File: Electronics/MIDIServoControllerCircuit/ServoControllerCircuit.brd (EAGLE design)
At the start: 160 x 100 mm, 19 parts, among them IC1 MCP1700INLINE, J1 PJ-063BH, T1 2N3904, X1 SIGNAL-PWR-GND, X2 SIGNAL-PWR-GND

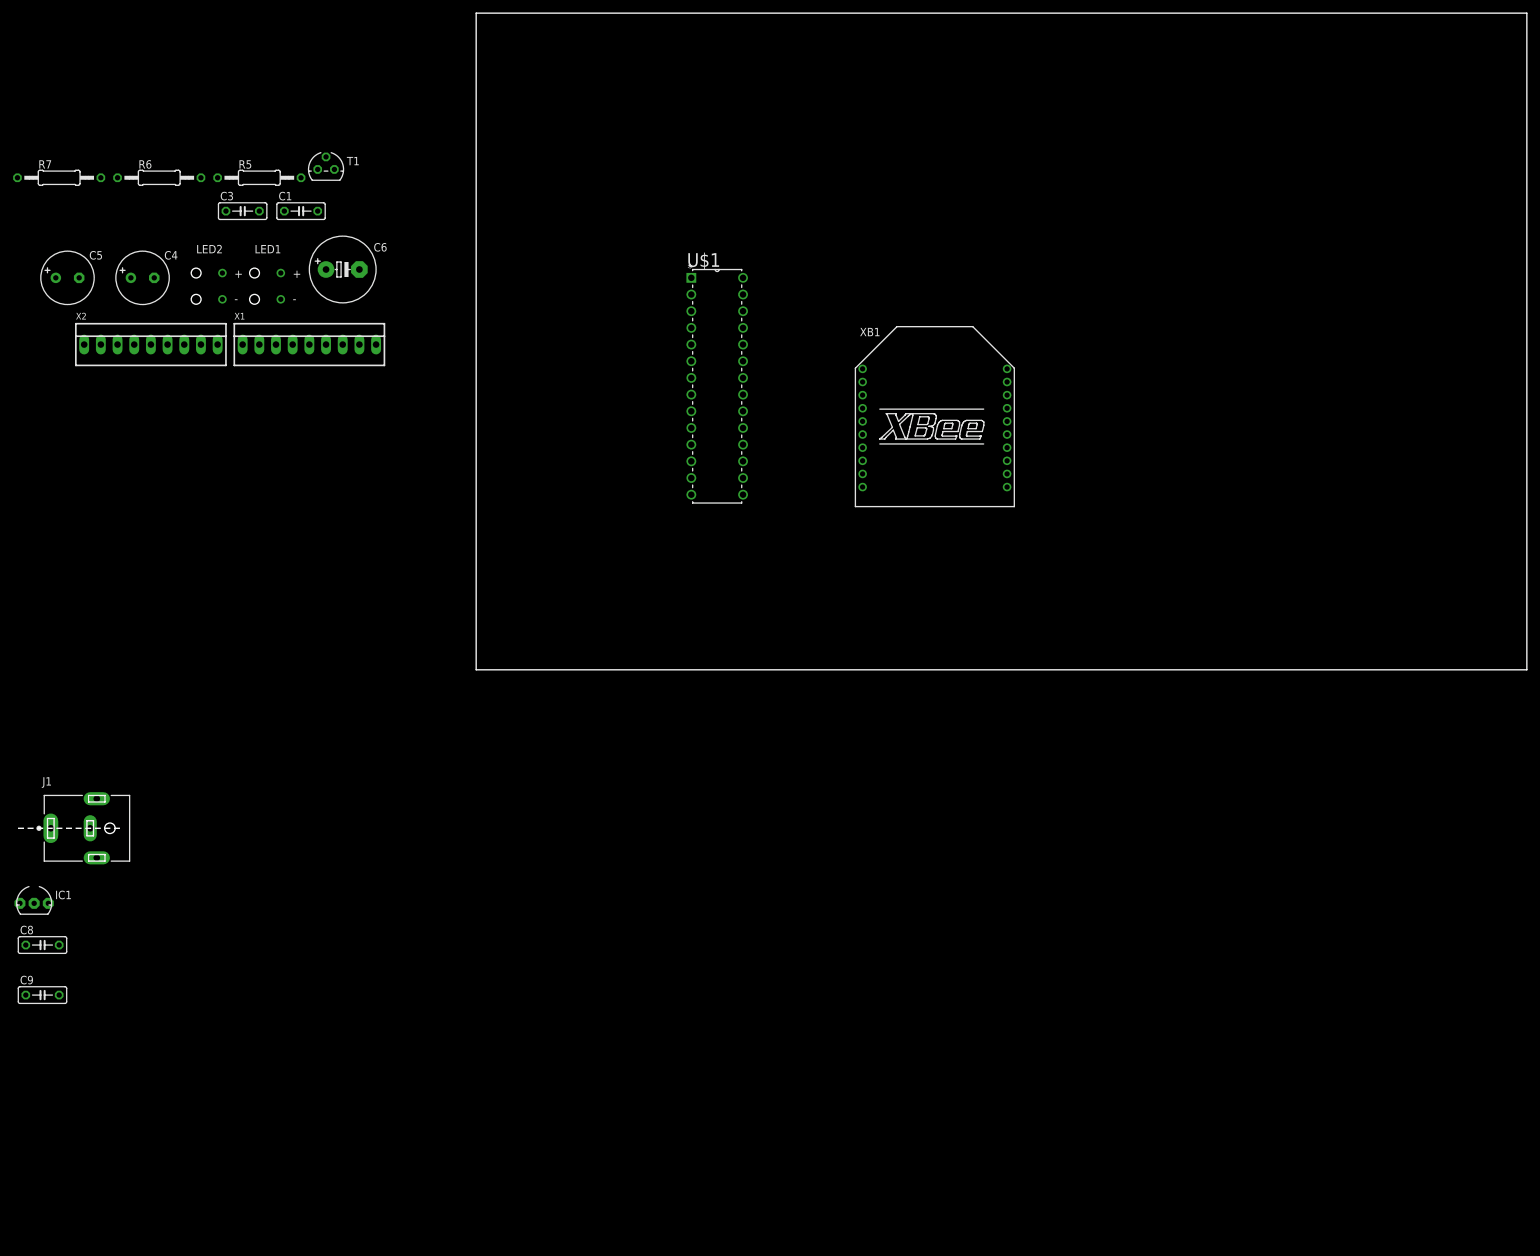
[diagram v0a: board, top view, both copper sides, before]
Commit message: Reversing modifications made to Electronics that are ahread of the rest of the project.
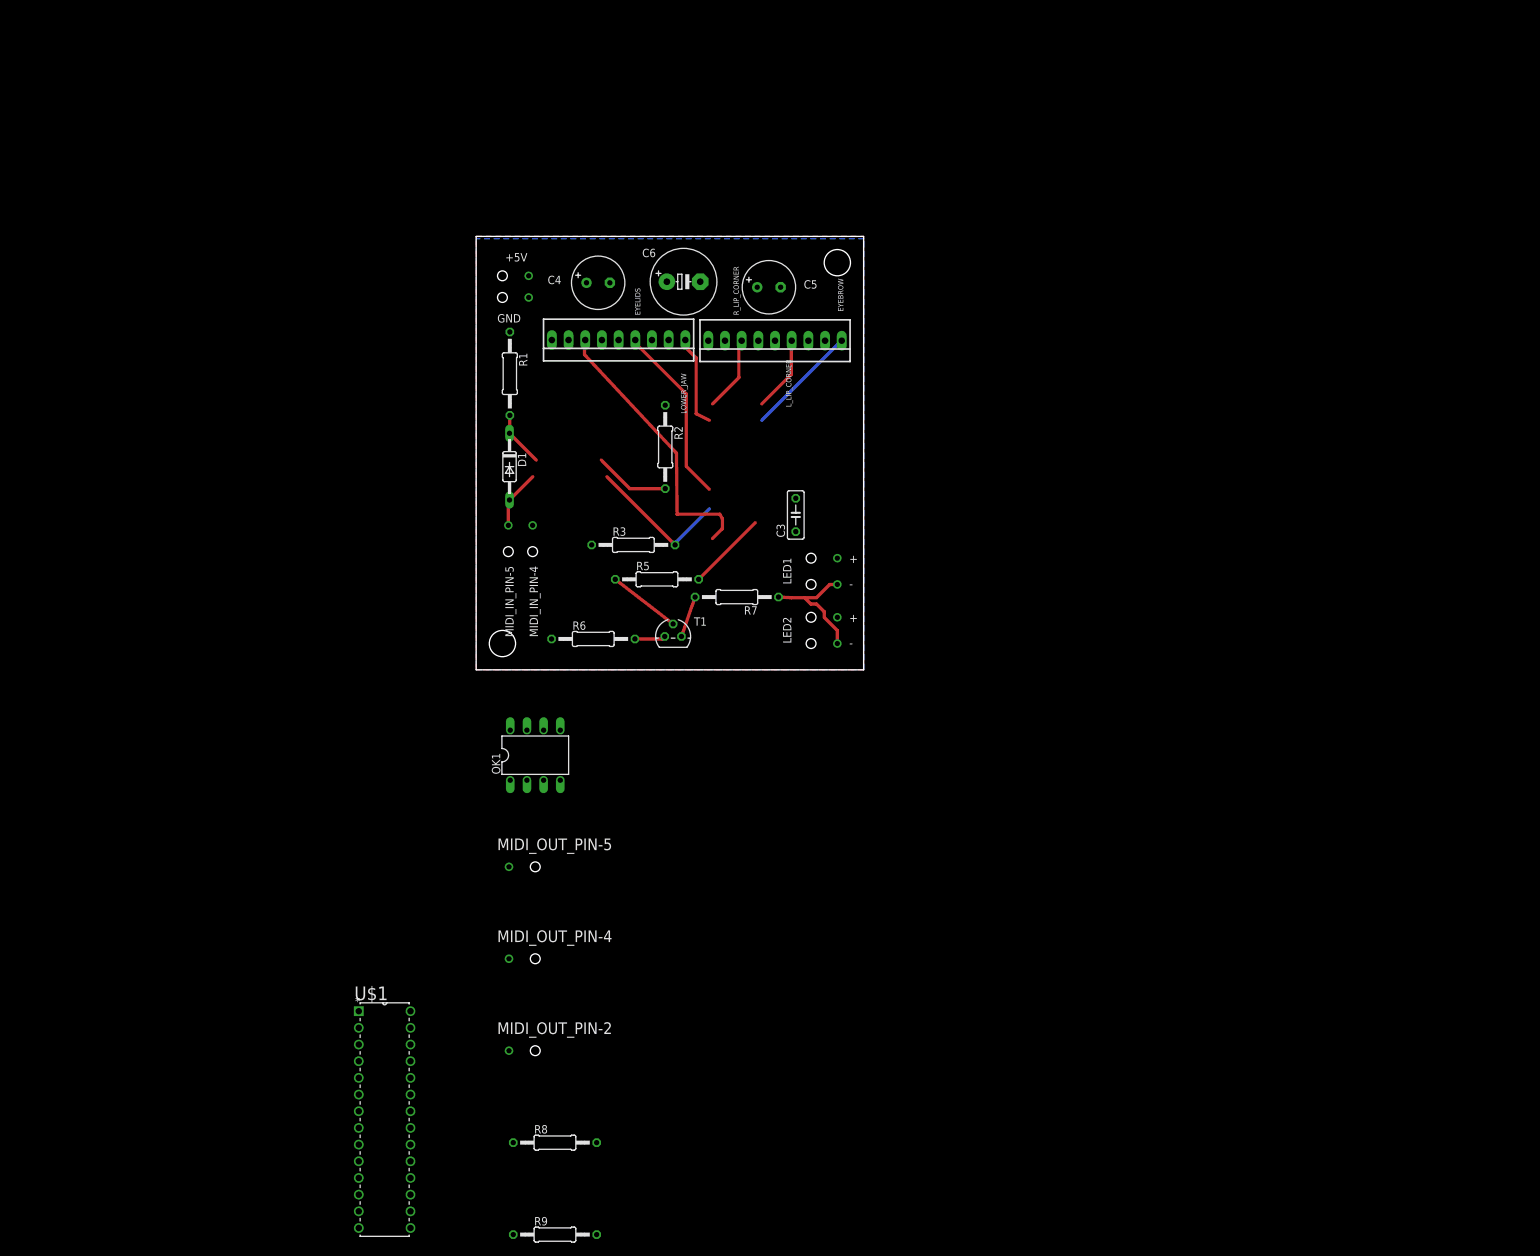
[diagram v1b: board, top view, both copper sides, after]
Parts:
- removed C1: 0.1u, resistor:C050-025X075
- removed C8, C9: 1u, resistor:C050-025X075
- removed IC1: MCP1700INLINE, MCP1700:TO92-INLINE
- removed J1: PJ-063BH, PJ-063BH:CUI_PJ-063BH
- removed XB1: XBEE, maxstream:XBEE
- added +5V, GND, MIDI_IN_PIN-4, MIDI_IN_PIN-5, MIDI_OUT_PIN-2, MIDI_OUT_PIN-4, MIDI_OUT_PIN-5: DOUBLE_THROUGH_HOLE_PAD, DOUBLE_THROUGH_HOLE_PAD:DOUBLE_THROUGH_HOLE_PAD
- added D1: 1N4148, diode:DO35-10
- added OK1: 6N138, optocoupler:DIL08
- added R1, R8, R9: 220, resistor:0207/12
- added R2: 4.7k, resistor:0207/12
- added R3: 270, resistor:0207/12
- moved U$1 122.6 mm to (-10.0, -85.0)
- moved R7 121.3 mm to (39.7, 11.1), turned to 180 degrees
- moved LED2 107.3 mm to (53.0, 6.00)
- moved C5 106.8 mm to (44.6, 58.3)
- moved R6 96.4 mm to (17.8, 4.70)
- moved C3 96.1 mm to (48.7, 23.6), turned to 90 degrees
- moved LED1 95.2 mm to (53.0, 15.0)
- moved X2 95.0 mm to (45.5, 50.1), turned to 180 degrees
- moved T1 88.6 mm to (30.0, 5.08)
- moved R5 86.1 mm to (27.5, 13.8)
- moved C4 69.4 mm to (18.6, 58.9)
- moved C6 51.9 mm to (31.6, 59.1)
- moved X1 47.1 mm to (21.7, 50.2), turned to 180 degrees
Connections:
- removed net +3.3V: C1.1, C8.2, IC1.3, XB1.1
- removed net PIC_RX: U$1.18, XB1.2
- removed net PIC_TX: U$1.17, XB1.3
- removed net SHIELD: J1.S1, J1.S2
- new net MIDI_PIN-5: D1.A, MIDI_IN_PIN-5.P$1, OK1.3
- new net N$1: D1.C, OK1.2, R1.2
- new net N$11: MIDI_OUT_PIN-4.P$1, R8.1
- new net N$2: OK1.7, R2.2
- new net RX_PIN: OK1.6, R3.2, U$1.18
- new net TX_PIN: R9.2, U$1.17
- net +5V: now also +5V.P$1, OK1.8, R3.1, R8.2; no longer C9.1, IC1.2, J1.1
- net GND: now also GND.P$1, MIDI_IN_PIN-4.P$1, MIDI_OUT_PIN-2.P$1, MIDI_OUT_PIN-5.P$1, OK1.5, R1.1, R2.1, R9.1; no longer C1.2, C8.1, C9.2, IC1.1, J1.2, XB1.10
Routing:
- net UNUSED: track 0.00 -> 43.0 mm
- net EYELIDS: track 0.00 -> 27.4 mm
- net RX_PIN: track 0.00 -> 22.3 mm
- net N$10: track 0.00 -> 19.4 mm
- net EYEBROW: track 0.00 -> 17.2 mm
- net LOWER_JAW: track 0.00 -> 14.1 mm
- net LIGHTS: track 0.00 -> 12.2 mm
- net RIGHT_LIP_CORNER: track 0.00 -> 11.6 mm
- net N$2: track 0.00 -> 11.5 mm
- net LEFT_LIP_CORNER: track 0.00 -> 11.5 mm
- net N$5: track 0.00 -> 11.1 mm
- net MIDI_PIN-5: track 0.00 -> 8.94 mm
- net N$1: track 0.00 -> 8.50 mm
- net N$9: track 0.00 -> 6.35 mm
- net N$7: track 0.00 -> 4.70 mm
- added copper zone on layer 1, net +5V
- added copper zone on layer 16, net GND
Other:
- board size 160 x 100 mm -> 59 x 66 mm
- board text added: "EYEBROW"
- board text added: "EYELIDS"
- board text added: "LOWER_JAW"
- board text added: "L_LIP_CORNER"
- board text added: "R_LIP_CORNER"

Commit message: Reversed modifications made to Electronics that are ahead of the rest of the project.
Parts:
- removed MIDI_OUT_PIN-2, MIDI_OUT_PIN-4, MIDI_OUT_PIN-5: DOUBLE_THROUGH_HOLE_PAD, DOUBLE_THROUGH_HOLE_PAD:DOUBLE_THROUGH_HOLE_PAD
- removed OK1: 6N138, optocoupler:DIL08
- removed R8, R9: 220, resistor:0207/12
- removed U$1: PIC18F24K40-I/SP, Microchip_By_element14_Batch_1:DIP254P762X508-28
- added 6N138: (no value), ic-package:SOCKET-08
- added C1, C2: 22p, resistor:C050-025X075
- added PIC16F628A: (no value), ic-package:SOCKET-18
- added Q1: 20MHz, special:QS
- added R4: 10k, resistor:0207/12
- renumbered MIDI_IN_PIN-4 to MIDI_PIN-4, MIDI_IN_PIN-5 to MIDI_PIN-5
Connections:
- removed net LOWER_JAW: U$1.5, X1.1
- removed net N$11: MIDI_OUT_PIN-4.P$1, R8.1
- removed net TX_PIN: R9.2, U$1.17
- new net LOWER_JAR: PIC16F628A.2, X1.1
- new net N$3: C1.1, PIC16F628A.16, Q1.2
- new net N$4: C2.1, PIC16F628A.15, Q1.1
- new net N$6: PIC16F628A.4, R4.2
- net +5V: now also 6N138.8, PIC16F628A.14, R4.1; no longer OK1.8, R8.2, U$1.20
- net EYEBROW: now also PIC16F628A.17; no longer U$1.2
- net EYELIDS: now also PIC16F628A.6; no longer U$1.6
- net GND: now also 6N138.5, C1.2, C2.2, PIC16F628A.5; no longer MIDI_OUT_PIN-2.P$1, MIDI_OUT_PIN-5.P$1, OK1.5, R9.1, U$1.19, U$1.8
- net LEFT_LIP_CORNER: now also PIC16F628A.18; no longer U$1.3
- net LIGHTS: now also PIC16F628A.11; no longer U$1.9
- net MIDI_PIN-5: now also 6N138.3; no longer OK1.3
- net N$1: now also 6N138.2; no longer OK1.2
- net N$2: now also 6N138.7; no longer OK1.7
- net RIGHT_LIP_CORNER: now also PIC16F628A.1; no longer U$1.4
- net RX_PIN: now also 6N138.6, PIC16F628A.7; no longer OK1.6, U$1.18
- net UNUSED: now also PIC16F628A.9; no longer U$1.7
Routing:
- net LOWER_JAR: track 0.00 -> 14.5 mm
- net LOWER_JAW: track 14.1 -> 0.00 mm
- net N$3: track 0.00 -> 13.9 mm
- net N$4: track 0.00 -> 12.2 mm
- net N$6: track 0.00 -> 11.3 mm
- net RX_PIN: track 22.3 -> 24.9 mm
- net MIDI_PIN-5: track 8.94 -> 10.5 mm
- net N$2: track 11.5 -> 12.8 mm
- net N$1: track 8.50 -> 9.50 mm
- net LIGHTS: track 12.2 -> 13.0 mm
